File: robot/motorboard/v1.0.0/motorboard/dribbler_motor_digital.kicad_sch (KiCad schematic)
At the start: 14 parts, among them J27 Conn_01x05_Female, U10 STSPIN32F0A

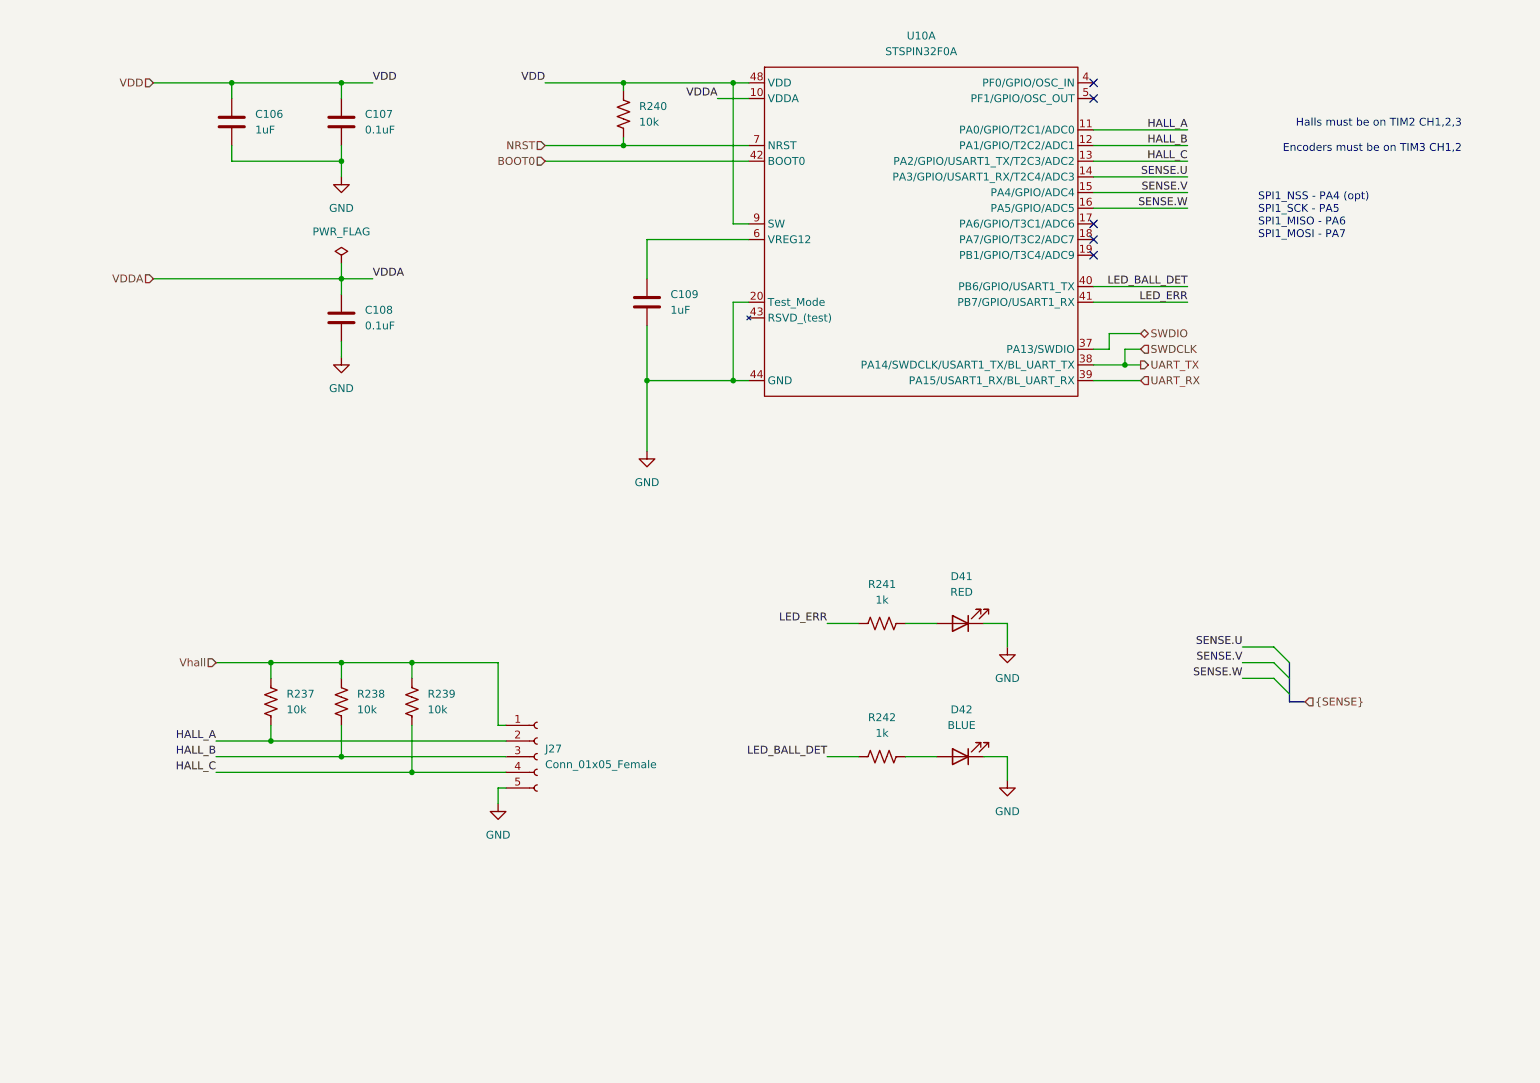
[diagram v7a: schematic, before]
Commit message: cleaned up remaining schematics
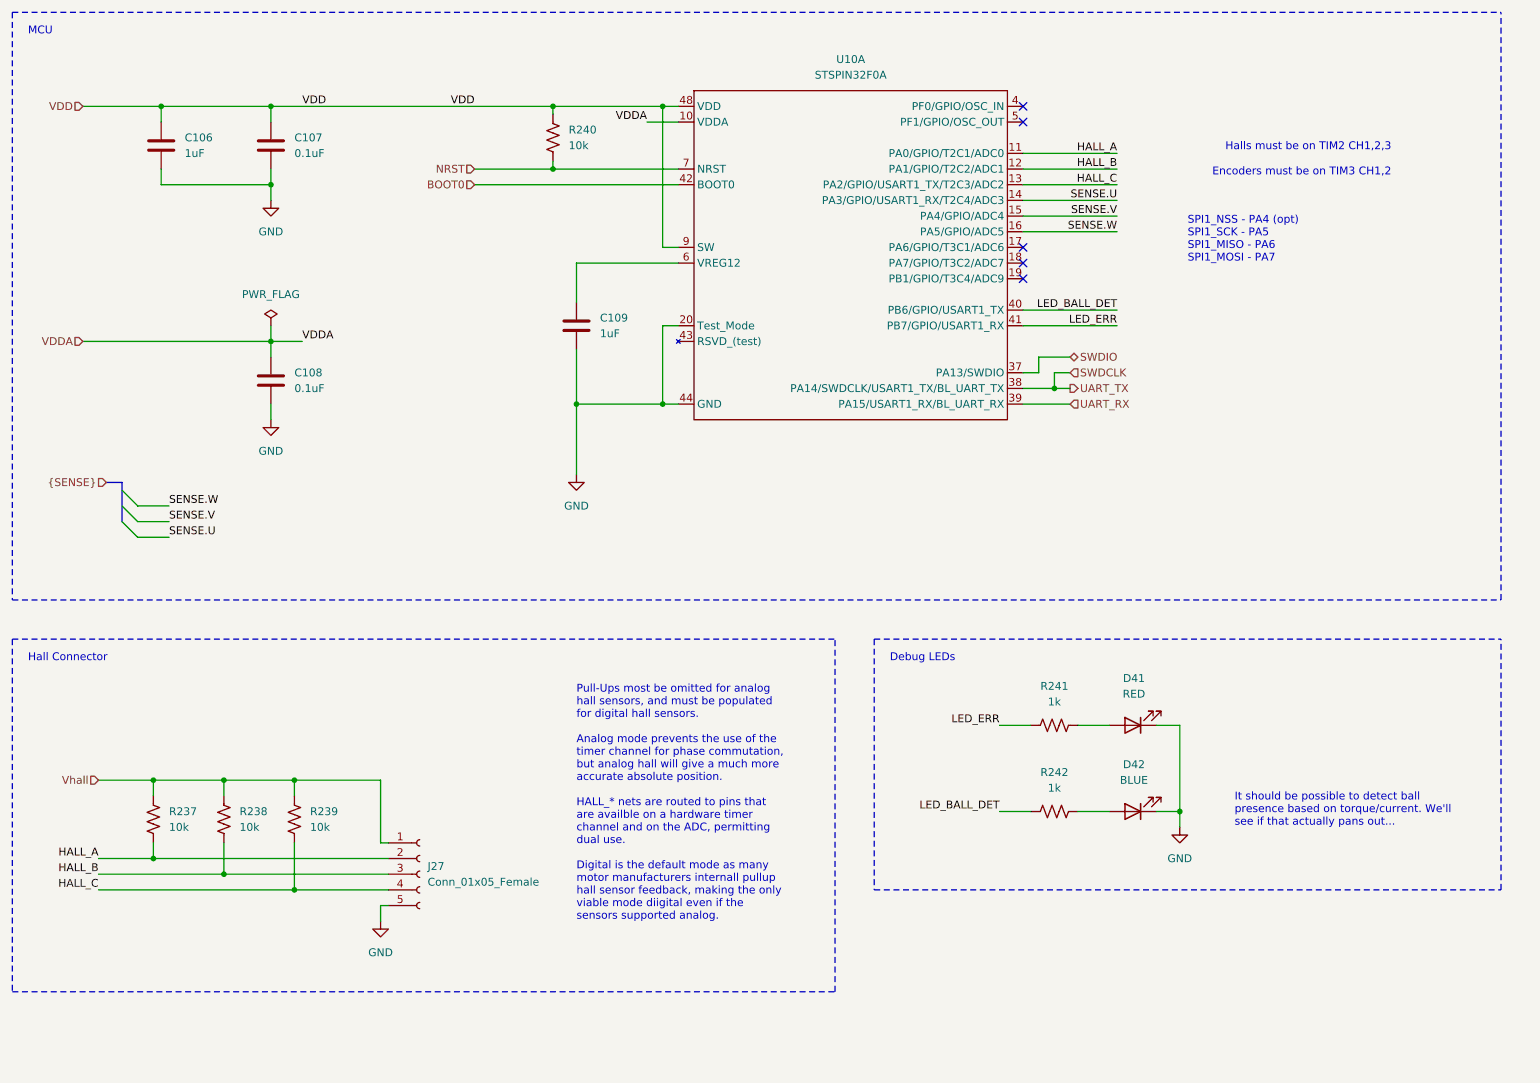
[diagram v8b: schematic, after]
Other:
- note added: "Debug LEDs"
- note added: "Hall Connector"
- note added: "It should be possible to detect ball presence based on torque/current. We'll see if that actually pans out..."
- note added: "MCU"
- note added: "Pull-Ups most be omitted for analog hall sensors, and must be populated for digital hall sensors. Analog mode prevents the use of the timer channel for phase commutation, but analog hall will give a much more accurate absolute position. HALL_* nets are routed to pins that are availble on a hardware timer channel and on the ADC, permitting dual use. Digital is the default mode as many motor manufa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"
- moved on the sheet: C106, C107, C108, C109, D41, D42, J27, R237, R238, R239, R240, R241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
